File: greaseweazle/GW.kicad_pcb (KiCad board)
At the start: 2 copper layers, 61 x 22.9 mm, 8 parts, among them P5 POWER

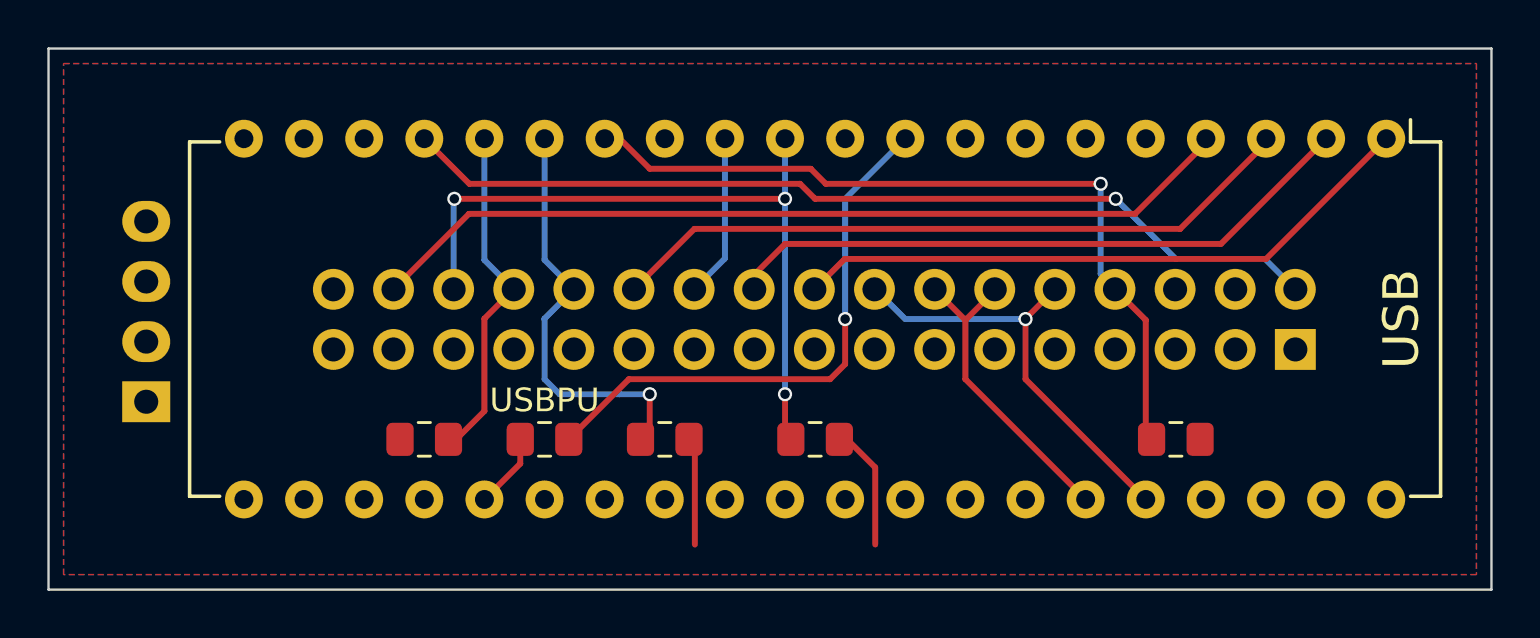
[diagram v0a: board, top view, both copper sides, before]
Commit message: made a THT version for easier soldering
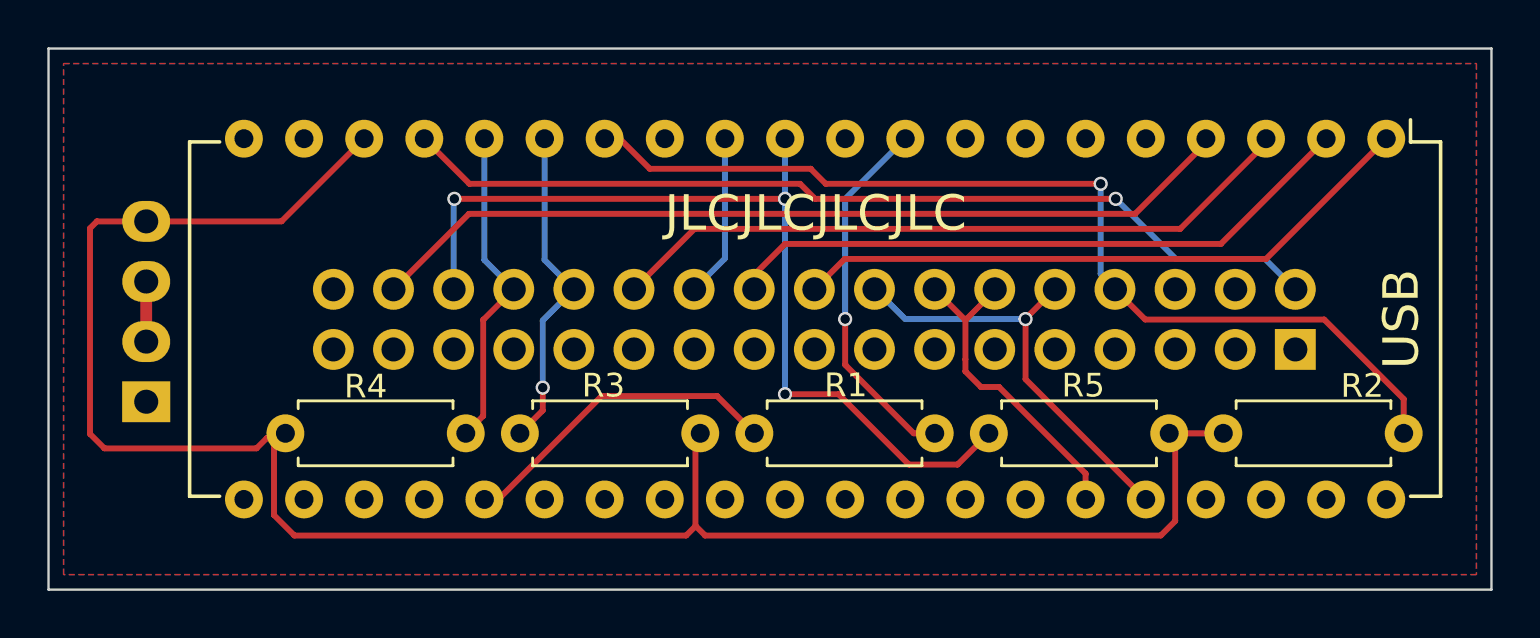
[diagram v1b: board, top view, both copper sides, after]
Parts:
- removed ? (x4): 1K, Resistor_SMD:R_0805_2012Metric_Pad1.15x1.40mm_HandSolder
- removed ?: , Housings_DIP:DIP-40_W15.24mm
- removed USBPU: 1.5K, Resistor_SMD:R_0805_2012Metric_Pad1.15x1.40mm_HandSolder
- added R1: 1.5K, Resistor_THT:R_Axial_DIN0207_L6.3mm_D2.5mm_P7.62mm_Horizontal, F.Cu at (146.7, 110.2)
- added R2: 1K, Resistor_THT:R_Axial_DIN0207_L6.3mm_D2.5mm_P7.62mm_Horizontal, F.Cu at (166.5, 110.2)
- added R3: 1K, Resistor_THT:R_Axial_DIN0207_L6.3mm_D2.5mm_P7.62mm_Horizontal, F.Cu at (144.4, 110.2)
- added R4: 1K, Resistor_THT:R_Axial_DIN0207_L6.3mm_D2.5mm_P7.62mm_Horizontal, F.Cu at (126.8, 110.2)
- added R5: 1K, Resistor_THT:R_Axial_DIN0207_L6.3mm_D2.5mm_P7.62mm_Horizontal, F.Cu at (164.2, 110.2)
- added U1: TAOBAO, Housings_DIP:DIP-40_W15.24mm, F.Cu at (173.4, 97.8)
- P7: renamed from ?; value (none) -> FLOPPY
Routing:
- net +5V: track 9.48 -> 83.7 mm
- net /USB_CONN: track 3.17 -> 13.9 mm
- net /_INDEX: track 33.4 -> 42.0 mm
- net /_DKRD: track 30.5 -> 39.0 mm
- net /USB_DP: track 23.6 -> 15.6 mm
- net /_TRK0: track 18.0 -> 13.9 mm
- net GND: track 0.00 -> 2.54 mm
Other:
- board text added: "JLCJLCJLCJLC"
